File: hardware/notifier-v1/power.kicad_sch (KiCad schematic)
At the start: 15 parts, among them J1 USB-C PWR/DATA, U2 USBLC6-2SC6, U3 TLV62569

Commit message: notifier-v1: USB 22 ohm series resistors, 1 uF at module 3V3, second buck output cap
Co-Authored-By: Claude Opus 5.5 <noreply@anthropic.com>
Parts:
- added C11: 22u, Capacitor_SMD:C_0805_2012Metric, symbol Device:C
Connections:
- net +3V3: now also C11.1
- net GND: now also C11.2
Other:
- note added: "Notes - Buck instead of LDO: from 5 V an LDO would burn about 0.6 W and warm the sensors. - USB D+/D- are a 90 ohm pair (0.25 mm / 0.15 mm gap): keep short, ESD diode U2 right at J1. - CC1/CC2 5.1k to GND: the host offers 5 V. VBUS_IN is before the polyfuse, VBUS after it. - Layout: buck bottom centre, far from the BME688; input cap C1 at VIN, output caps at L1. - Output caps: C2 + C11 22 uF 0805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"
- note removed: "Notes - Buck instead of LDO: from 5 V an LDO would burn about 0.6 W and warm the sensors. - USB D+/D- are a 90 ohm pair (0.25 mm / 0.15 mm gap): keep short, ESD diode U2 right at J1. - CC1/CC2 5.1k to GND: the host offers 5 V. VBUS_IN is before the polyfuse, VBUS after it. - Layout: buck bottom centre, far from the BME688; input cap C1 at VIN, output caps at L1."
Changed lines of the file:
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@@
+	)
+	(symbol
+		(lib_id "Device:C")
+		(at 284.48 109.22 0)
+		(unit 1)
+		(exclude_from_sim no)
+		(in_bom yes)
+		(on_board yes)
+		(dnp no)
+		(fields_autoplaced no)
+		(property "Reference" "C11"
+			(at 286.68 107.92 0)
+			(effects
+				(font
+					(size 1.27 1.27)
+				) (justify left)
+			)
+		)
+		(property "Value" "22u"
+			(at 286.68 110.52 0)
+			(effects
+				(font
+					(size 1.27 1.27)
+				) (justify left)
+			)
+		)
+		(property "Footprint" "Capacitor_SMD:C_0805_2012Metric"
+			(at 285.4452 105.41 0.0000)
+			(effects
+				(font
+					(size 1.27 1.27)
+				)
+				(hide yes)
+			)
+		)
+		(property "LCSC" "C45783"
+			(at 287.02 114.2999 0)
+			(effects
+				(font
+					(size 1.27 1.27)
+				)
+				(justify left) (hide yes)
+			)
+		)
+		(pin "1"
+		)
+		(pin "2"
+		)
+		(instances
+			(project "notifier-v1"
+				(path "/85cf2753-6181-5f74-b525-c66aecc4c100/8981c1c3-ff50-5488-808f-726a0ebb5885"
+					(reference "C11")
+					(unit 1)
+				)
+			)
+		)
 	)
 	(symbol
@@
 	(symbol
 		(lib_id "power:PWR_FLAG")
-		(at 284.48 99.06 0)
+		(at 294.64 99.06 0)
 		(unit 1)
 		(exclude_from_sim no)
@@
 		(fields_autoplaced no)
 		(property "Reference" "#FLG03"
-			(at 284.48 100.965 0.0000)
+			(at 294.64 100.965 0.0000)
 			(effects
 				(font
@@
 		)
 		(property "Value" "PWR_FLAG"
-			(at 284.48 93.98 0)
+			(at 294.64 93.98 0)
 			(effects
 				(font
@@
 	(wire (pts (xy 226.06 115.57) (xy 248.92 115.57)) (stroke (width 0) (type default)))
 	(wire (pts (xy 248.92 125.73) (xy 248.92 129.54)) (stroke (width 0) (type default)))
+	(wire (pts (xy 284.48 105.41) (xy 284.48 99.06)) (stroke (width 0) (type default)))
 	(wire (pts (xy 264.16 105.41) (xy 264.16 99.06)) (stroke (width 0) (type default)))
 	(wire (pts (xy 274.32 105.41) (xy 274.32 99.06)) (stroke (width 0) (type default)))
@@
 	(wire (pts (xy 264.16 119.38) (xy 274.32 119.38)) (stroke (width 0) (type default)))
 	(wire (pts (xy 274.32 119.38) (xy 274.32 113.03)) (stroke (width 0) (type default)))
+	(wire (pts (xy 274.32 119.38) (xy 284.48 119.38)) (stroke (width 0) (type default)))
+	(wire (pts (xy 284.48 119.38) (xy 284.48 113.03)) (stroke (width 0) (type default)))
 	(wire (pts (xy 269.24 119.38) (xy 269.24 127.0)) (stroke (width 0) (type default)))
 	(wire (pts (xy 187.96 71.12) (xy 187.96 105.41)) (stroke (width 0) (type default)))
@@
 	(junction (at 269.24 119.38) (diameter 0) (color 0 0 0 0))
 	(junction (at 274.32 99.06) (diameter 0) (color 0 0 0 0))
+	(junction (at 274.32 119.38) (diameter 0) (color 0 0 0 0))
 	(junction (at 284.48 99.06) (diameter 0) (color 0 0 0 0))
+	(junction (at 294.64 99.06) (diameter 0) (color 0 0 0 0))
 	(junction (at 299.72 99.06) (diameter 0) (color 0 0 0 0))
 	(rectangle (start 25.4 55.88) (end 147.32 142.24) (stroke (width 0.2) (type dash)) (fill (type none)))
@@
 	(text "Power LED" (exclude_from_sim no) (at 321.31 77.22 0) (effects (font (size 1.5 1.5) bold) (justify left top)))
 	(label "LED_A" (at 320.04 115.57 0) (effects (font (size 1.27 1.27)) (justify left)))
-	(text "Notes\n- Buck instead of LDO: from 5 V an LDO would burn about 0.6 W and warm the sensors.\n- USB D+/D- are a 90 ohm pair (0.25 mm / 0.15 mm gap): keep short, ESD diode U2 right at J1.\n- CC1/CC2 5.1k to GND: the host offers 5 V. VBUS_IN is before the polyfuse, VBUS after it.\n- Layout: buck bottom centre, far from the BME688; input cap C1 at VIN, output caps at L1." (exclude_from_sim no) (at 35.56 157.48 0) (effects (font (size 1.27 1.27)) (justify left top)))
+	(text "Notes\n- Buck instead of LDO: from 5 V an LDO would burn about 0.6 W and warm the sensors.\n- USB D+/D- are a 90 ohm pair (0.25 mm / 0.15 mm gap): keep short, ESD diode U2 right at J1.\n- CC1/CC2 5.1k to GND: the host offers 5 V. VBUS_IN is before the polyfuse, VBUS after it.\n- Layout: buck bottom centre, far from the BME688; input cap C1 at VIN, output caps at L1.\n- Output caps: C2 + C11 22 uF 0805 derate to about 11 uF each at 3.3 V; TLV62569 wants 10-47 uF effective." (exclude_from_sim no) (at 35.56 157.48 0) (effects (font (size 1.27 1.27)) (justify left top)))
 	(sheet_instances
 		(path "/"

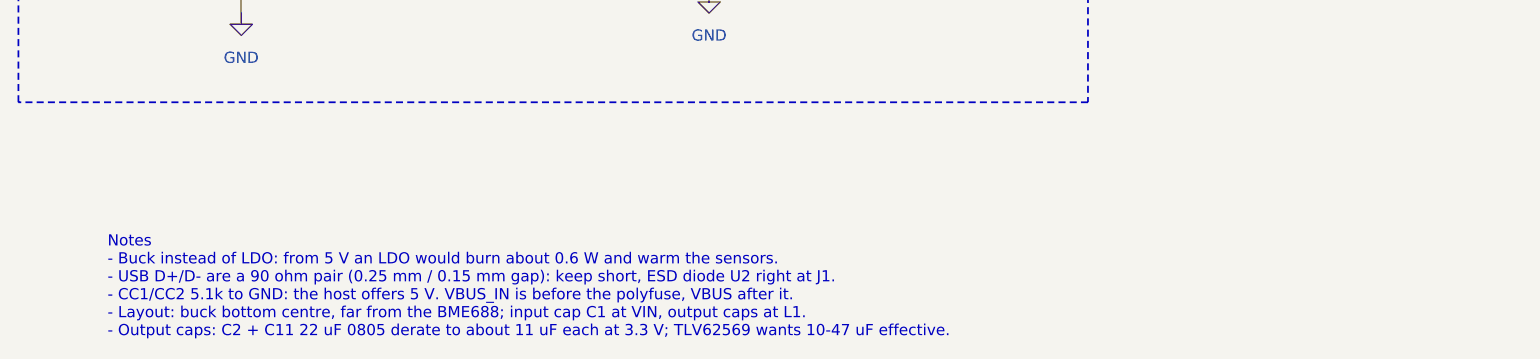
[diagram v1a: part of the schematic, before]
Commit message: notifier-v1: 90 ohm USB pair, hand-drawn and locked
USB D+/D- are 0.27 mm with a 0.15 mm gap on F.Cu over the In1 GND plane: 90 ohm
differential on JLC04161H-7628 (prepreg 0.2104 mm, er 4.4, 1 oz, solder mask).
The router left the pair partial (interleaved USB-C pads) and snaked it over
B.Cu with ~8 vias; drawing it in layout_v1.py makes it straight, via-free and
the pipeline passed 4 of 4 runs (was ~1 of 3).

- U2 (USBLC6) rotated 270 for flow-through; VBUS_IN/GND middle pins by via
- module-side nets renamed MCU_USB_DP/MCU_USB_DN (KRT pairs by suffix)
- route_krt.sh: diff stage dropped, --keep-input-copper
- ORDER.md: calculator inputs to verify; hw-layout skill updated

Co-Authored-By: Claude Opus 5.5 <noreply@anthropic.com>
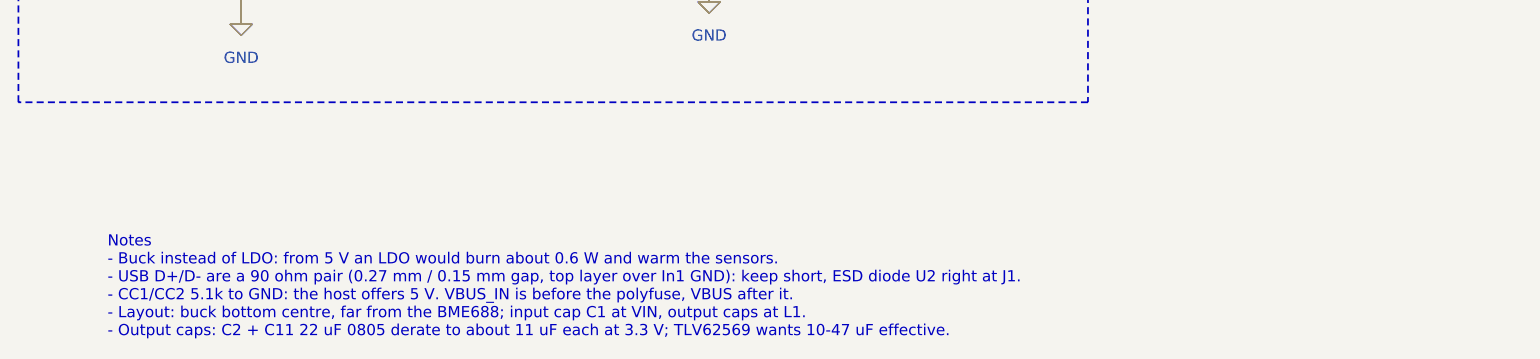
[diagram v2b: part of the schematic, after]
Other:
- note added: "Notes - Buck instead of LDO: from 5 V an LDO would burn about 0.6 W and warm the sensors. - USB D+/D- are a 90 ohm pair (0.27 mm / 0.15 mm gap, top layer over In1 GND): keep short, ESD diode U2 right at J1. - CC1/CC2 5.1k to GND: the host offers 5 V. VBUS_IN is before the polyfuse, VBUS after it. - Layout: buck bottom centre, far from the BME688; input cap C1 at VIN, output caps at L1. - Output c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"
- note removed: "Notes - Buck instead of LDO: from 5 V an LDO would burn about 0.6 W and warm the sensors. - USB D+/D- are a 90 ohm pair (0.25 mm / 0.15 mm gap): keep short, ESD diode U2 right at J1. - CC1/CC2 5.1k to GND: the host offers 5 V. VBUS_IN is before the polyfuse, VBUS after it. - Layout: buck bottom centre, far from the BME688; input cap C1 at VIN, output caps at L1. - Output caps: C2 + C11 22 uF 0805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"
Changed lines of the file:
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@@
 	(text "Power LED" (exclude_from_sim no) (at 321.31 77.22 0) (effects (font (size 1.5 1.5) bold) (justify left top)))
 	(label "LED_A" (at 320.04 115.57 0) (effects (font (size 1.27 1.27)) (justify left)))
-	(text "Notes\n- Buck instead of LDO: from 5 V an LDO would burn about 0.6 W and warm the sensors.\n- USB D+/D- are a 90 ohm pair (0.25 mm / 0.15 mm gap): keep short, ESD diode U2 right at J1.\n- CC1/CC2 5.1k to GND: the host offers 5 V. VBUS_IN is before the polyfuse, VBUS after it.\n- Layout: buck bottom centre, far from the BME688; input cap C1 at VIN, output caps at L1.\n- Output caps: C2 + C11 22 uF 0805 derate to about 11 uF each at 3.3 V; TLV62569 wants 10-47 uF effective." (exclude_from_sim no) (at 35.56 157.48 0) (effects (font (size 1.27 1.27)) (justify left top)))
+	(text "Notes\n- Buck instead of LDO: from 5 V an LDO would burn about 0.6 W and warm the sensors.\n- USB D+/D- are a 90 ohm pair (0.27 mm / 0.15 mm gap, top layer over In1 GND): keep short, ESD diode U2 right at J1.\n- CC1/CC2 5.1k to GND: the host offers 5 V. VBUS_IN is before the polyfuse, VBUS after it.\n- Layout: buck bottom centre, far from the BME688; input cap C1 at VIN, output caps at L1.\n- Output caps: C2 + C11 22 uF 0805 derate to about 11 uF each at 3.3 V; TLV62569 wants 10-47 uF effective." (exclude_from_sim no) (at 35.56 157.48 0) (effects (font (size 1.27 1.27)) (justify left top)))
 	(sheet_instances
 		(path "/"

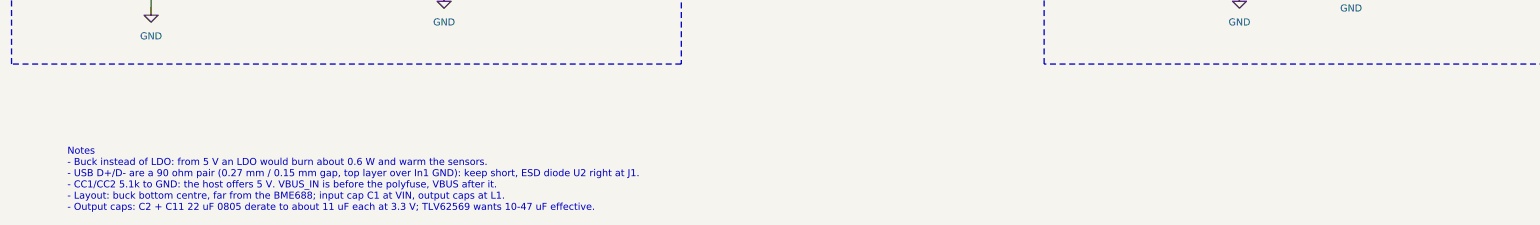
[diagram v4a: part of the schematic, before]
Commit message: Layout A: USB-C on the back edge, corner mounts, no buttons, JLC fab data
- J2 display socket mirrored (1 RST 2 CS 3 DC 4 SDA 5 SCL 6 GND 7 VCC),
  face at the right edge
- USB-C J1 on the left edge (enclosure back), ESD/CC/fuse beside it,
  hand-drawn 0.27/0.15 pair (~91 ohm diff, tools/impedance.py), only
  GND under the shell (DRC rule area)
- SW1-SW3/R6/BTN removed; 1.5 mm debug pads TX RX 3V3 EN GND IO0;
  firmware DESK_BTN = -1 on notifier-v1
- Four M2 corner holes with keepouts; sensor island grown to 14.8 mm
  with H3 in its corner, re-hand-routed (BME688/SHT40 8.9 mm apart)
- I2C >= 1.6 mm from USB on the same layer; vias >= 0.15 mm from
  same-net SMD pads (rule), hand vias >= 0.2 mm
- Silk "v1 ${GIT_SHA}" resolved at fab export; JLC order-number mark
- Fab: Protel gerbers without X2, PTH/NPTH split, JLC BOM/CPL, CPL
  rotation fixes (U4 +90, U5 +270); pipeline --fab-only on a clean
  commit; route retry until the gate passes
- ORDER.md: stackup JLC04161H-7628, rails left/right, preview checklist,
  bring-up without buttons; PLAN.md enclosure notes

Co-Authored-By: Claude Opus 5.5 <noreply@anthropic.com>
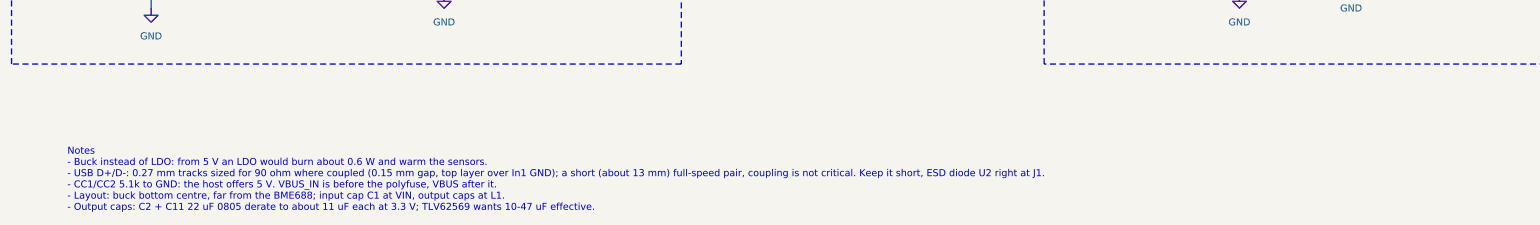
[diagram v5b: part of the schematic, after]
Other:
- note added: "Notes - Buck instead of LDO: from 5 V an LDO would burn about 0.6 W and warm the sensors. - USB D+/D-: 0.27 mm tracks sized for 90 ohm where coupled (0.15 mm gap, top layer over In1 GND); a short (about 13 mm) full-speed pair, coupling is not critical. Keep it short, ESD diode U2 right at J1. - CC1/CC2 5.1k to GND: the host offers 5 V. VBUS_IN is before the polyfuse, VBUS after it. - Layout: buck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"
- note removed: "Notes - Buck instead of LDO: from 5 V an LDO would burn about 0.6 W and warm the sensors. - USB D+/D- are a 90 ohm pair (0.27 mm / 0.15 mm gap, top layer over In1 GND): keep short, ESD diode U2 right at J1. - CC1/CC2 5.1k to GND: the host offers 5 V. VBUS_IN is before the polyfuse, VBUS after it. - Layout: buck bottom centre, far from the BME688; input cap C1 at VIN, output caps at L1. - Output c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"
